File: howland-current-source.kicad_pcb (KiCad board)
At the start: 2 copper layers, 10 parts

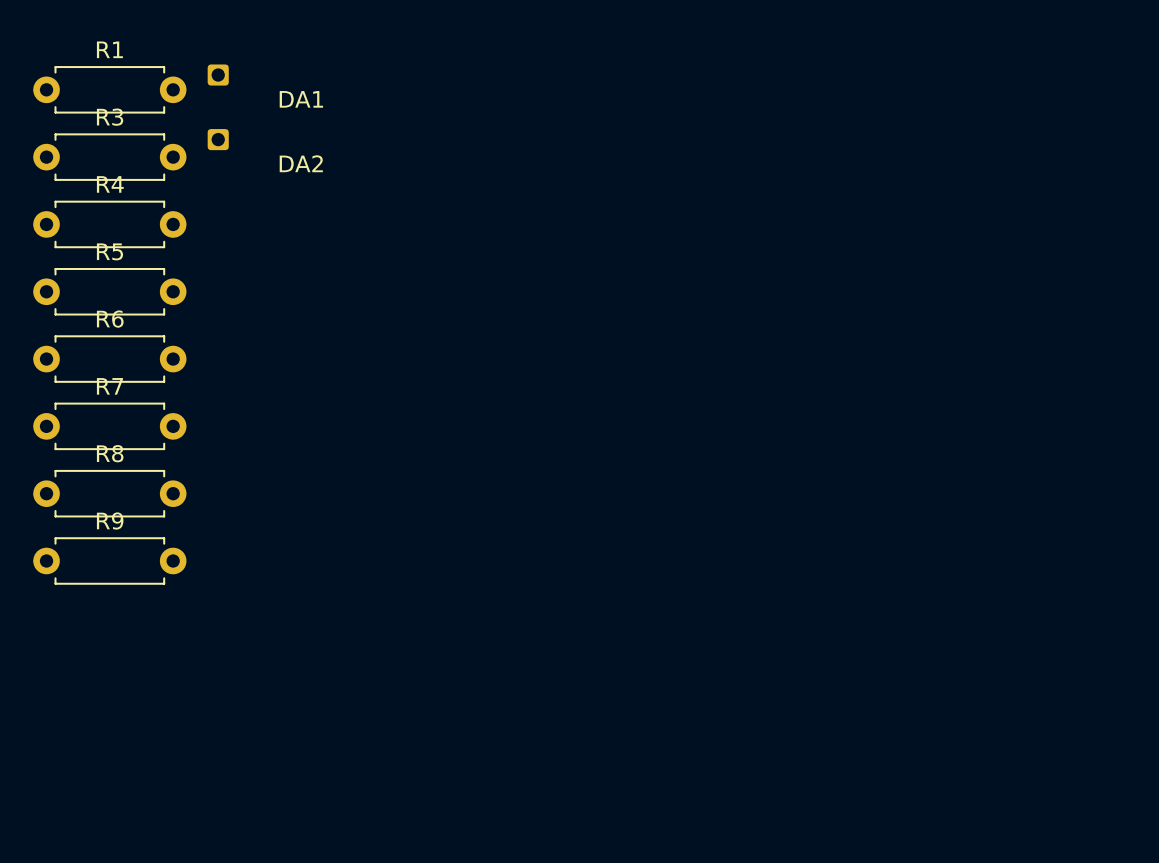
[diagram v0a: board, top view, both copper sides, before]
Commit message: Add PCB layout with routing complete
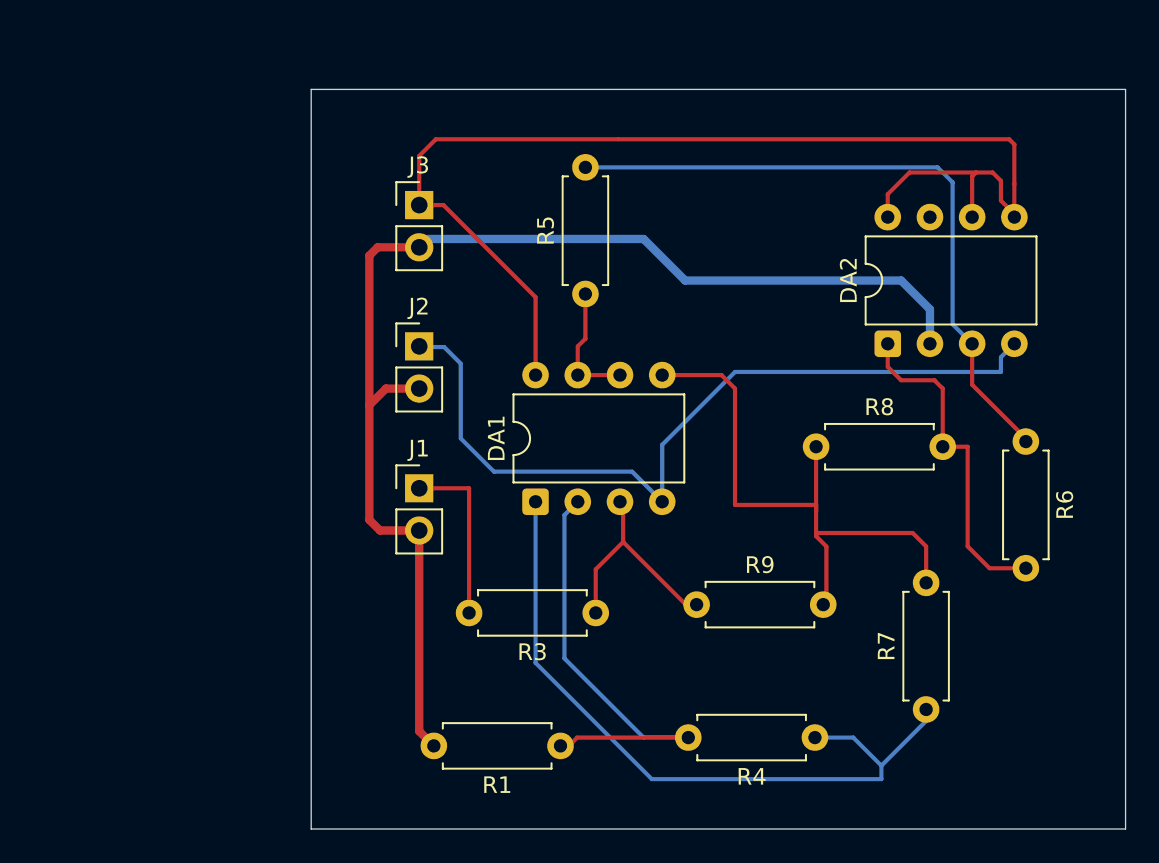
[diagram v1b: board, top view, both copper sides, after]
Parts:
- added J1: Conn_01x02, Connector_PinHeader_2.54mm:PinHeader_1x02_P2.54mm_Vertical, F.Cu at (42.0, 108.0)
- added J2: Conn_01x02, Connector_PinHeader_2.54mm:PinHeader_1x02_P2.54mm_Vertical, F.Cu at (42.0, 99.5)
- added J3: Conn_01x02, Connector_PinHeader_2.54mm:PinHeader_1x02_P2.54mm_Vertical, F.Cu at (42.0, 91.0)
- DA1, DA2: footprint howland_gost_footprints:OPA2277_DIP8 -> Package_DIP:DIP-8_W7.62mm
- moved R6 59.1 mm to (78.5, 105.2), turned to -90 degrees
- moved R7 55.6 mm to (72.5, 121.3), turned to 90 degrees
- moved R4 55.6 mm to (65.8, 123.0), turned to 180 degrees
- moved R1 50.1 mm to (50.5, 123.5), turned to 180 degrees
- moved R8 46.4 mm to (65.9, 105.5)
- moved R3 42.9 mm to (52.6, 115.5), turned to 180 degrees
- moved R9 39.2 mm to (58.7, 115.0)
- moved DA2 36.8 mm to (70.2, 99.3), turned to 90 degrees
- moved R5 32.4 mm to (52.0, 96.3), turned to 90 degrees
- moved DA1 27.6 mm to (49.0, 108.8), turned to 90 degrees
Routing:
- net GND: track 0.00 -> 73.9 mm
- net +12V: track 0.00 -> 71.2 mm
- net -12V: track 0.00 -> 48.8 mm
- net Net-(DA1A-Out): track 0.00 -> 43.4 mm
- net Net-(DA2A-In+): track 0.00 -> 39.4 mm
- net Net-(DA1B-In+): track 0.00 -> 36.1 mm
- net Net-(DA1A-In-): track 0.00 -> 27.1 mm
- net Net-(DA2A-Out): track 0.00 -> 20.3 mm
- net Net-(DA1A-In+): track 0.00 -> 13.4 mm
- net Net-(J1-Pin_1): track 0.00 -> 10.7 mm
- net Net-(DA1B-In-): track 0.00 -> 7.61 mm
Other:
- board outline added: 49 x 44.5 mm
